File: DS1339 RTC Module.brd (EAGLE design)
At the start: 24.1 x 17.4 mm, 12 parts, among them U1 DS1339AU, Y1 ECS-.327-6-17X-TR

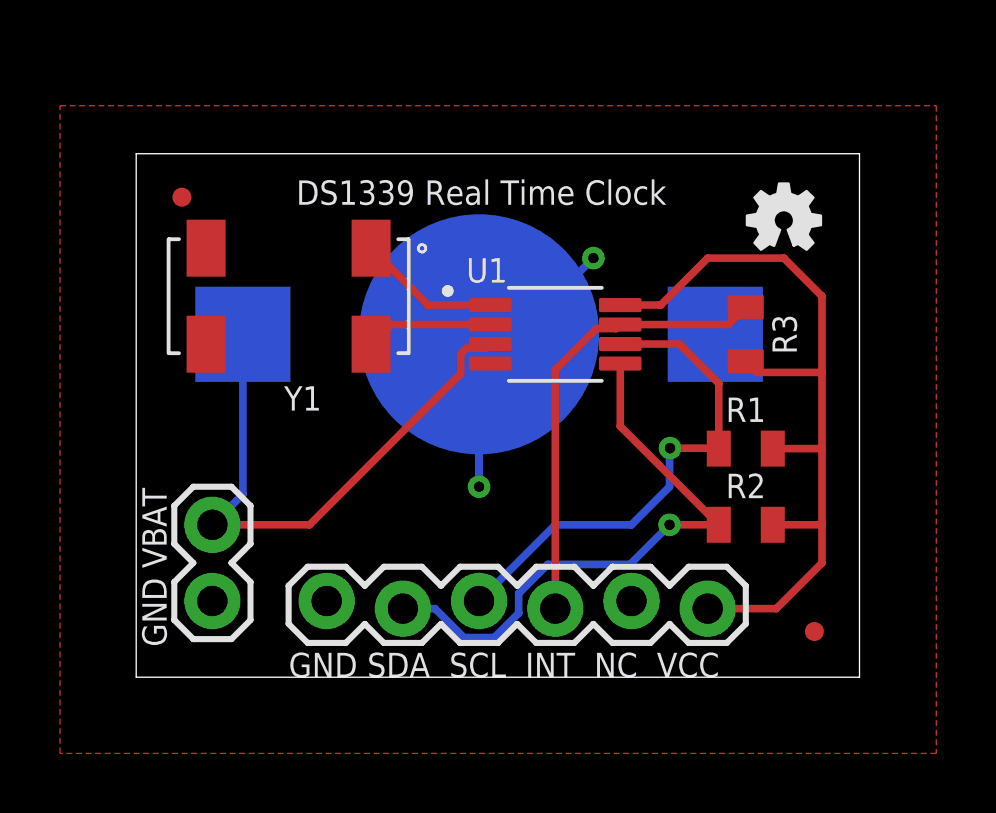
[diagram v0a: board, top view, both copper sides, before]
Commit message: Oops - Flipped VCC and GND on connector
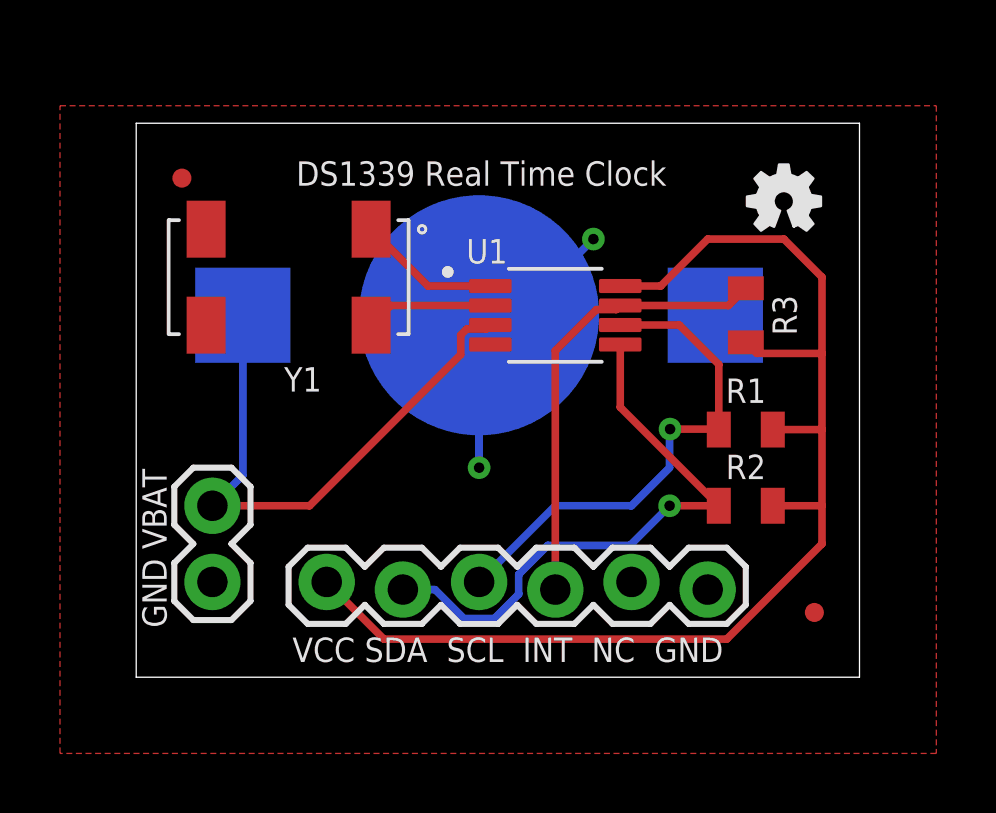
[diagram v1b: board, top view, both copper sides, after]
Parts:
- moved FD2 0.64 mm to (1.52, 16.6)
- moved Y1 0.64 mm to (5.08, 13.3)
- moved R1 0.64 mm to (20.3, 8.26)
- moved CR1225 0.63 mm to (11.4, 12.1)
- moved FD1 0.63 mm to (22.6, 2.16)
- moved J1 0.63 mm to (6.35, 3.17)
- moved J2 0.63 mm to (2.54, 3.17)
- moved LOGO1 0.63 mm to (21.6, 15.9)
- moved R2 0.63 mm to (20.3, 5.71)
- moved R3 0.63 mm to (20.3, 12.1)
- moved U1 0.63 mm to (14.0, 12.1)
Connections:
- net GND: now also J1.6; no longer J1.1
- net VCC: now also J1.1; no longer J1.6
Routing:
- net VCC: track 27.2 -> 41.4 mm
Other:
- board size 24.1 x 17.4 mm -> 24.1 x 18.5 mm
- board text added: "VCC SDA SCL INT NC GND"
- board text removed: "GND SDA SCL INT NC VCC"

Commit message: Fine Tuned some routing
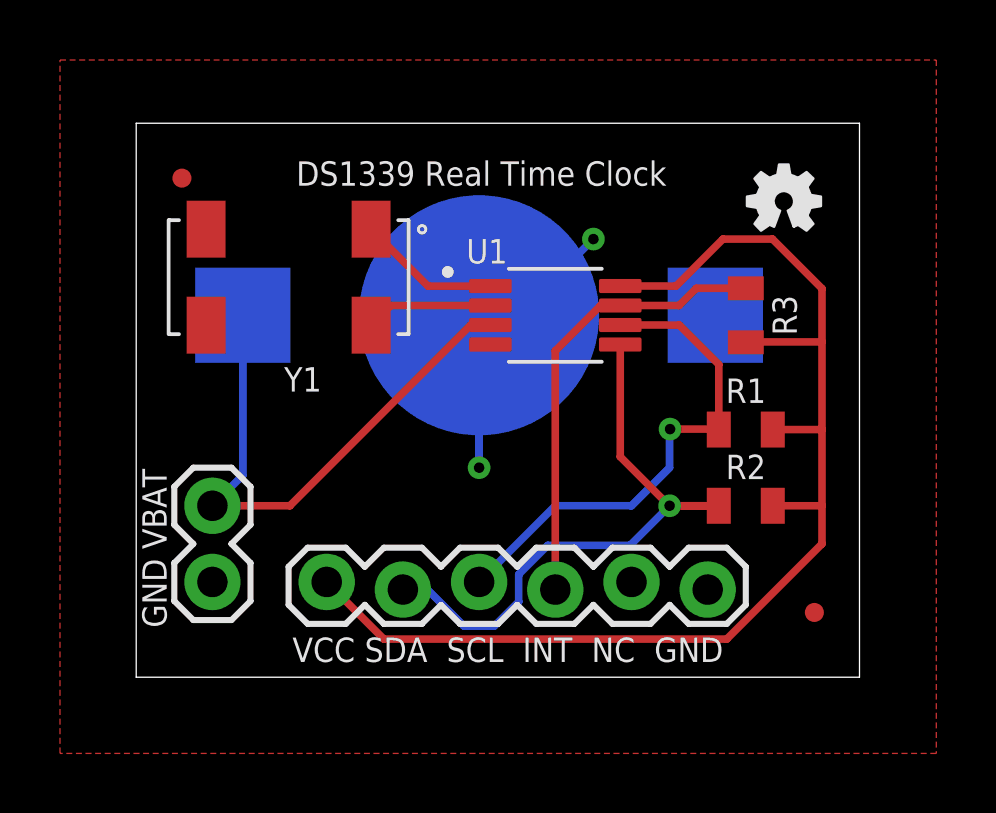
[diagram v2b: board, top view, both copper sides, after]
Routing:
- net SDA: track 19.6 -> 20.9 mm
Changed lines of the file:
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@@
 <contactref element="R3" pad="2"/>
 <contactref element="R2" pad="2"/>
-<wire x1="16.135" y1="13.04" x2="17.485" y2="13.04" width="0.254" layer="1"/>
-<wire x1="17.485" y1="13.04" x2="19.05" y2="14.605" width="0.254" layer="1"/>
-<wire x1="19.05" y1="14.605" x2="21.59" y2="14.605" width="0.254" layer="1"/>
-<wire x1="21.59" y1="14.605" x2="22.86" y2="13.335" width="0.254" layer="1"/>
+<wire x1="16.135" y1="13.04" x2="17.993" y2="13.04" width="0.254" layer="1"/>
+<wire x1="17.993" y1="13.04" x2="19.558" y2="14.605" width="0.254" layer="1"/>
+<wire x1="19.558" y1="14.605" x2="21.209" y2="14.605" width="0.254" layer="1"/>
+<wire x1="21.209" y1="14.605" x2="22.86" y2="12.954" width="0.254" layer="1"/>
 <wire x1="22.86" y1="8.255" x2="22.86" y2="5.715" width="0.254" layer="1"/>
 <wire x1="22.86" y1="5.715" x2="22.86" y2="4.445" width="0.254" layer="1"/>
 <wire x1="21.22" y1="5.715" x2="22.86" y2="5.715" width="0.254" layer="1"/>
 <wire x1="21.22" y1="8.255" x2="22.86" y2="8.255" width="0.254" layer="1"/>
-<wire x1="22.86" y1="13.335" x2="22.86" y2="10.795" width="0.254" layer="1"/>
-<wire x1="22.86" y1="10.795" x2="22.86" y2="8.255" width="0.254" layer="1"/>
-<wire x1="22.86" y1="10.795" x2="20.69" y2="10.795" width="0.254" layer="1"/>
-<wire x1="20.69" y1="10.795" x2="20.32" y2="11.165" width="0.254" layer="1"/>
+<wire x1="22.86" y1="12.954" x2="22.86" y2="11.176" width="0.254" layer="1"/>
+<wire x1="22.86" y1="11.176" x2="22.86" y2="8.255" width="0.254" layer="1"/>
+<wire x1="20.32" y1="11.165" x2="20.331" y2="11.176" width="0.254" layer="1"/>
+<wire x1="22.86" y1="11.176" x2="20.331" y2="11.176" width="0.254" layer="1"/>
 <contactref element="J1" pad="1"/>
 <wire x1="19.685" y1="1.27" x2="8.255" y2="1.27" width="0.254" layer="1"/>
@@
 <contactref element="Y1" pad="2"/>
 <polygon width="0.254" layer="1">
-<vertex x="-2.54" y="19.05"/>
-<vertex x="26.67" y="19.05"/>
+<vertex x="-2.54" y="20.574"/>
+<vertex x="26.67" y="20.574"/>
 <vertex x="26.67" y="-2.54"/>
 <vertex x="-2.54" y="-2.54"/>
@@
 <contactref element="R3" pad="1"/>
 <contactref element="U1" pad="7"/>
-<wire x1="16.135" y1="12.39" x2="19.745" y2="12.39" width="0.254" layer="1"/>
-<wire x1="19.745" y1="12.39" x2="20.32" y2="12.965" width="0.254" layer="1"/>
-<wire x1="16.135" y1="12.39" x2="15.9994" y2="12.2544" width="0.254" layer="1"/>
-<wire x1="15.9994" y1="12.2544" x2="15.34368125" y2="12.2544" width="0.254" layer="1"/>
-<wire x1="15.34368125" y1="12.2544" x2="13.97" y2="10.88071875" width="0.254" layer="1"/>
+<wire x1="16.135" y1="12.39" x2="18.094" y2="12.39" width="0.254" layer="1"/>
+<wire x1="18.669" y1="12.965" x2="18.094" y2="12.39" width="0.254" layer="1"/>
+<wire x1="18.669" y1="12.965" x2="20.32" y2="12.965" width="0.254" layer="1"/>
+<wire x1="16.135" y1="12.39" x2="16.1264" y2="12.3814" width="0.254" layer="1"/>
+<wire x1="16.1264" y1="12.3814" x2="15.47068125" y2="12.3814" width="0.254" layer="1"/>
+<wire x1="15.47068125" y1="12.3814" x2="13.97" y2="10.88071875" width="0.254" layer="1"/>
 <wire x1="13.97" y1="10.88071875" x2="13.97" y2="2.921" width="0.254" layer="1"/>
 </signal>
@@
 <contactref element="R2" pad="1"/>
 <contactref element="U1" pad="5"/>
-<wire x1="16.135" y1="11.09" x2="16.135" y2="9" width="0.254" layer="1"/>
-<wire x1="16.135" y1="9" x2="19.42" y2="5.715" width="0.254" layer="1"/>
-<wire x1="10.9249875" y1="1.9558" x2="11.9350125" y2="1.9558" width="0.254" layer="16"/>
+<wire x1="16.135" y1="11.09" x2="16.135" y2="7.349" width="0.254" layer="1"/>
+<wire x1="17.769" y1="5.715" x2="19.42" y2="5.715" width="0.254" layer="1"/>
+<wire x1="17.769" y1="5.715" x2="16.135" y2="7.349" width="0.254" layer="1"/>
+<wire x1="10.9249875" y1="1.7018" x2="11.9350125" y2="1.7018" width="0.254" layer="16"/>
 <wire x1="16.4592" y1="4.3942" x2="17.78" y2="5.715" width="0.254" layer="16"/>
-<wire x1="8.89" y1="2.921" x2="9.9597875" y2="2.921" width="0.254" layer="16"/>
-<wire x1="9.9597875" y1="2.921" x2="10.9249875" y2="1.9558" width="0.254" layer="16"/>
-<wire x1="11.9350125" y1="1.9558" x2="12.7508" y2="2.7715875" width="0.254" layer="16"/>
-<wire x1="12.7508" y1="2.7715875" x2="12.7508" y2="3.4260125" width="0.254" layer="16"/>
+<wire x1="8.89" y1="2.921" x2="9.7057875" y2="2.921" width="0.254" layer="16"/>
+<wire x1="9.7057875" y1="2.921" x2="10.9249875" y2="1.7018" width="0.254" layer="16"/>
+<wire x1="11.9350125" y1="1.7018" x2="12.7508" y2="2.5175875" width="0.254" layer="16"/>
+<wire x1="12.7508" y1="2.5175875" x2="12.7508" y2="3.4260125" width="0.254" layer="16"/>
 <wire x1="12.7508" y1="3.4260125" x2="13.7189875" y2="4.3942" width="0.254" layer="16"/>
 <wire x1="13.7189875" y1="4.3942" x2="16.4592" y2="4.3942" width="0.254" layer="16"/>
@@
 <contactref element="U1" pad="3"/>
 <contactref element="CR1225" pad="PWR@2"/>
-<wire x1="5.78" y1="5.715" x2="2.54" y2="5.715" width="0.254" layer="1"/>
-<wire x1="11.805" y1="11.74" x2="11.6694" y2="11.6044" width="0.254" layer="1"/>
-<wire x1="11.6694" y1="11.6044" x2="11.01368125" y2="11.6044" width="0.254" layer="1"/>
-<wire x1="11.01368125" y1="11.6044" x2="10.8156" y2="11.40631875" width="0.254" layer="1"/>
-<wire x1="10.8156" y1="10.7506" x2="5.78" y2="5.715" width="0.254" layer="1"/>
-<wire x1="10.8156" y1="11.40631875" x2="10.8156" y2="10.7506" width="0.254" layer="1"/>
+<wire x1="5.12428125" y1="5.715" x2="2.54" y2="5.715" width="0.254" layer="1"/>
+<wire x1="11.805" y1="11.74" x2="11.7964" y2="11.7314" width="0.254" layer="1"/>
+<wire x1="11.7964" y1="11.7314" x2="11.14068125" y2="11.7314" width="0.254" layer="1"/>
+<wire x1="11.14068125" y1="11.7314" x2="5.12428125" y2="5.715" width="0.254" layer="1"/>
 <wire x1="3.556" y1="12.065" x2="3.556" y2="6.731" width="0.254" layer="16"/>
 <wire x1="3.556" y1="6.731" x2="2.54" y2="5.715" width="0.254" layer="16"/>
